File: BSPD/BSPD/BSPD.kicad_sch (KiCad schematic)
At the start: 10 parts, among them Q1 NMOS, U1 LM397, U2 LM397, U3 74AHC1G08, U4 74AHC1G02

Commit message: Timer and relay added/updated
Added timer circuit and 12v relay that we used from shutdown pcb
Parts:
- removed R1, R3: R_Small_US, symbol Device:R_Small_US
- added C1: 0.1u, symbol Device:C
- added K1: AZ943-1CH-12DE, AZ943-1CH_AMZ, symbol AZ943_1CH_12DE:AZ943-1CH-12DE
- added R5: 1M, symbol Device:R
- added R6: 523k, symbol Device:R
- added R7: 768k, symbol Device:R
- added RV1, RV2: 1k, symbol Device:R_Potentiometer
- added U5: LTC6994CS6-1-TRMPBF, TSOT-23_S6_LIT, symbol LTC6994:LTC6994CS6-1-TRMPBF
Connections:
- net GND: now also C1.2, R6.2, R7.2, U5.2 (GND)
- net at R2.1, U2.1 (-): now also RV2.3
- net at U4.4: now also U5.1 (IN)
- net at R4.1, U1.1 (-): now also RV1.3
- net at D1.1 (K): now also K1.5
- net at D1.2 (A), Q1.1 (D): now also K1.2
- net at Q1.2 (G): now also U5.6 (OUT)
- new net: R7.1, U5.3 (SET)
- new net: R5.2, R6.1, U5.4 (DIV)
- new net +5V: C1.1, R5.1, RV1.2, RV2.2, U5.5 (V+)
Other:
- moved on the sheet: D1, Q1, U4

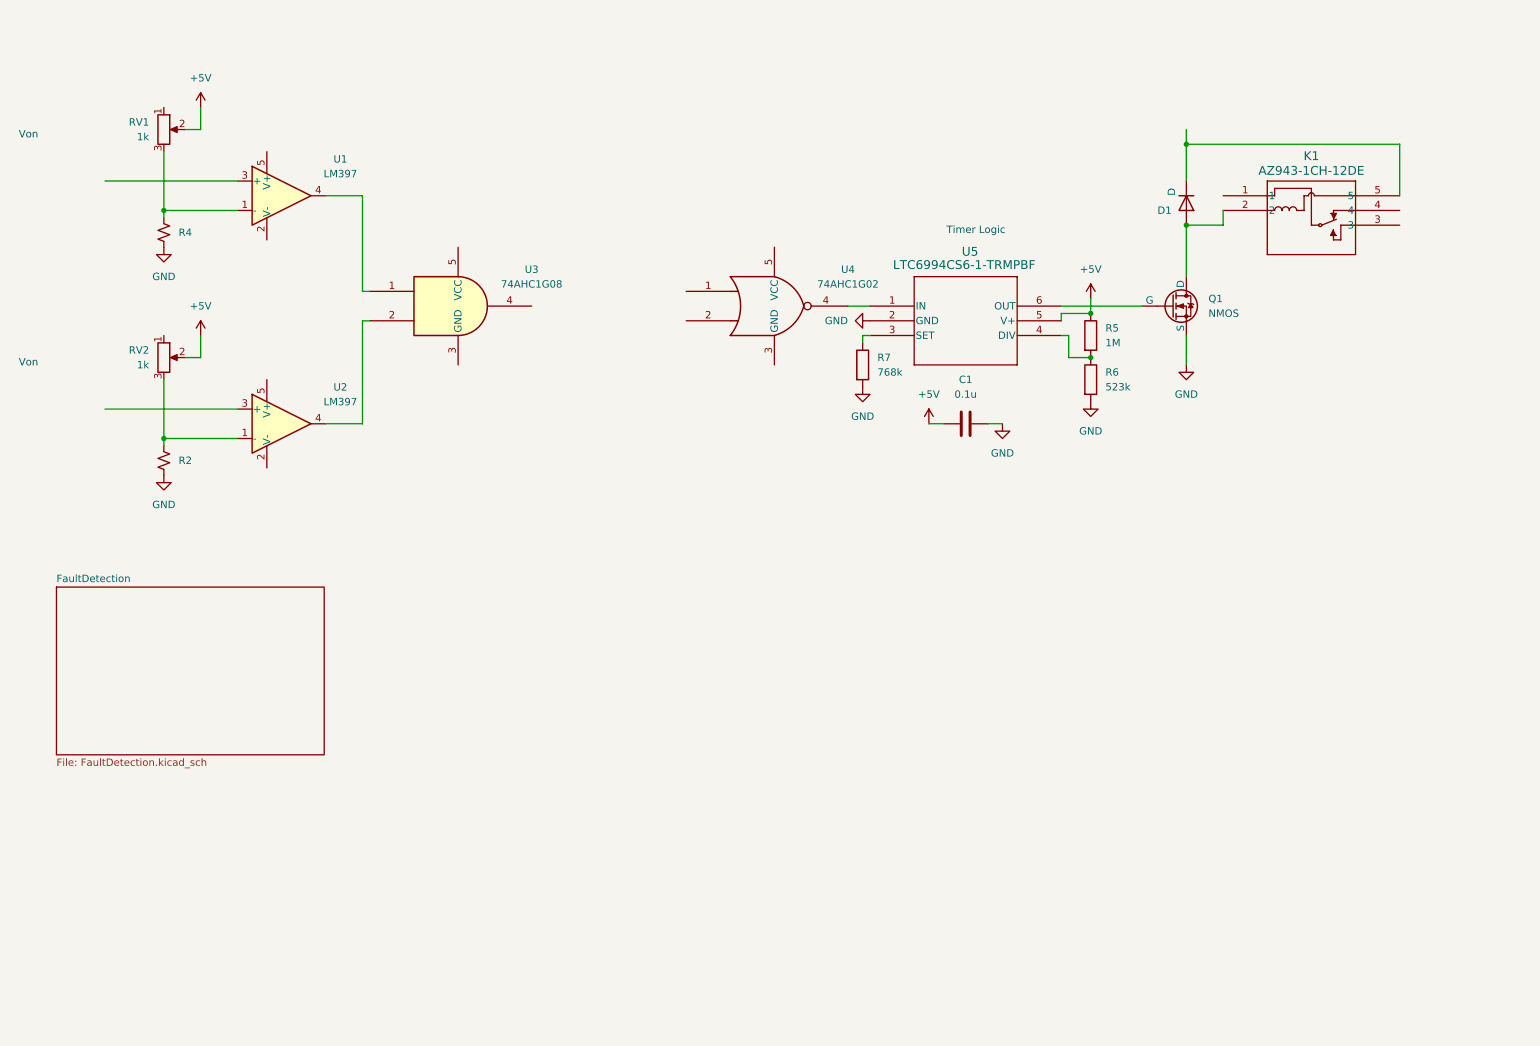
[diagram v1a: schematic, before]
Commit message: Relay Driver/Regulator/IO/LEDS/Comparator
Added relay driver, 5v regulator, debugging leds, 6 pin microfit connector for IO, and created footprint for TLV7012DDFR comparator we're using
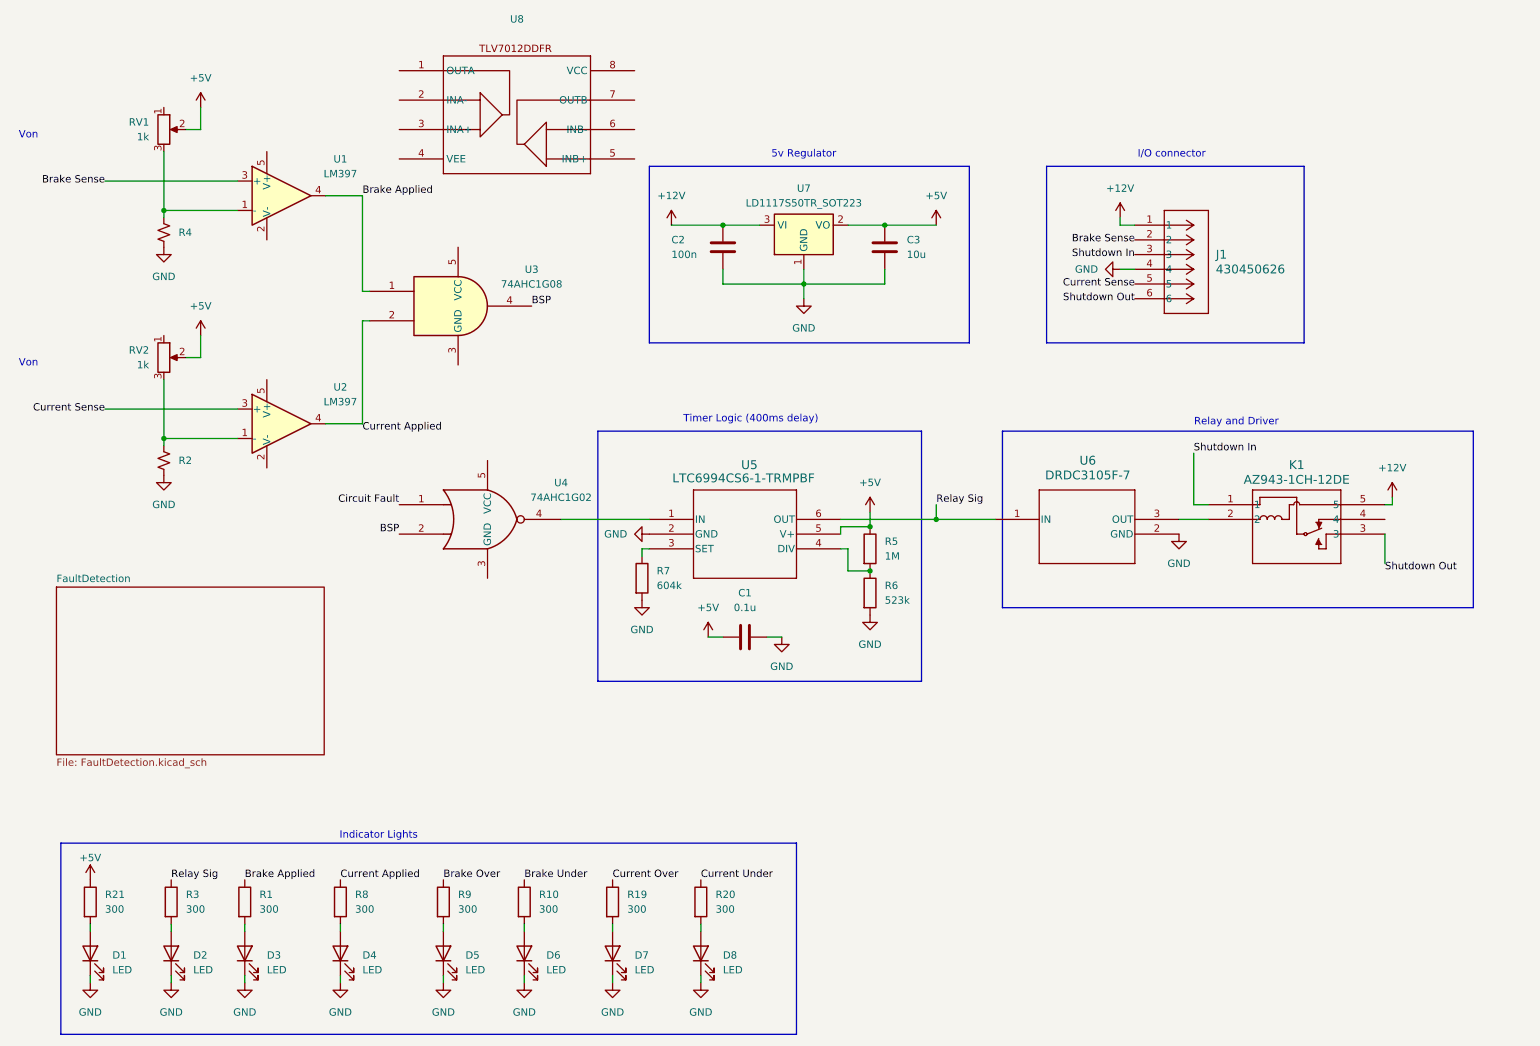
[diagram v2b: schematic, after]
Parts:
- removed D1: D, symbol Device:D
- removed Q1: NMOS, symbol Simulation_SPICE:NMOS
- added C2: 100n, symbol Device:C
- added C3: 10u, symbol Device:C
- added D1, D2, D3, D4, D5, D6, D7, D8: LED, symbol Device:LED
- added J1: 430450626, CONN_SD-43045-009_06_MOL, symbol Molex_430450626:430450626
- added R1, R10, R19, R20, R21, R3, R8, R9: 300, symbol Device:R
- added U6: DRDC3105F-7, SOT23_DIO, symbol DRDC3105:DRDC3105F-7
- added U7: LD1117S50TR_SOT223, Package_TO_SOT_SMD:SOT-223-3_TabPin2, symbol Regulator_Linear:LD1117S50TR_SOT223
- added U8: ~, symbol TLV7012DDFR:TLV7012DDFR
- R7: value 768k -> 604k
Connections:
- net +5V: now also C3.1, R21.1, U7.2 (VO)
- net GND: now also C2.2, C3.2, D1.1 (K), D2.1 (K), D3.1 (K), D4.1 (K), D5.1 (K), D6.1 (K), D7.1 (K), D8.1 (K), J1.4, U6.2 (GND), U7.1 (GND)
- net Current Sense: now reaches U2.3 (+)
- net Current Sense: now also J1.5
- net Current Applied: now reaches U2.4, U3.2
- net Current Applied: now also R8.1
- net Circuit Fault: now reaches U4.1
- net BSP: now reaches U4.2
- net BSP: now also U3.4
- net Brake Sense: now reaches U1.3 (+)
- net Brake Sense: now also J1.2
- net Brake Applied: now reaches U1.4, U3.1
- net Brake Applied: now also R1.1
- net +12V: now reaches K1.5
- net +12V: now also C2.1, J1.1, U7.3 (VI)
- net at K1.2: now also U6.3 (OUT)
- net Relay Sig: now reaches U5.6 (OUT)
- net Relay Sig: now also R3.1, U6.1 (IN)
- net Shutdown In: now reaches K1.1
- net Shutdown In: now also J1.3
- net Shutdown Out: now reaches K1.3
- net Shutdown Out: now also J1.6
- new net: D7.2 (A), R19.2
- new net: D8.2 (A), R20.2
- new net: D2.2 (A), R3.2
- new net: D6.2 (A), R10.2
- new net: D5.2 (A), R9.2
- new net: D4.2 (A), R8.2
- new net: D1.2 (A), R21.2
- new net: D3.2 (A), R1.2
- new net Brake Over: R9.1
- new net Brake Under: R10.1
- new net Current Over: R19.1
- new net Current Under: R20.1
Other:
- note added: "5v Regulator"
- note added: "I/O connector"
- note added: "Indicator Lights"
- note added: "Relay and Driver"
- note added: "Timer Logic (400ms delay)"
- note removed: "Timer Logic"
- title: (none) -> BSPD
- moved on the sheet: C1, K1, R5, R6, R7, U4, U5

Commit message: Added logic gate symbols
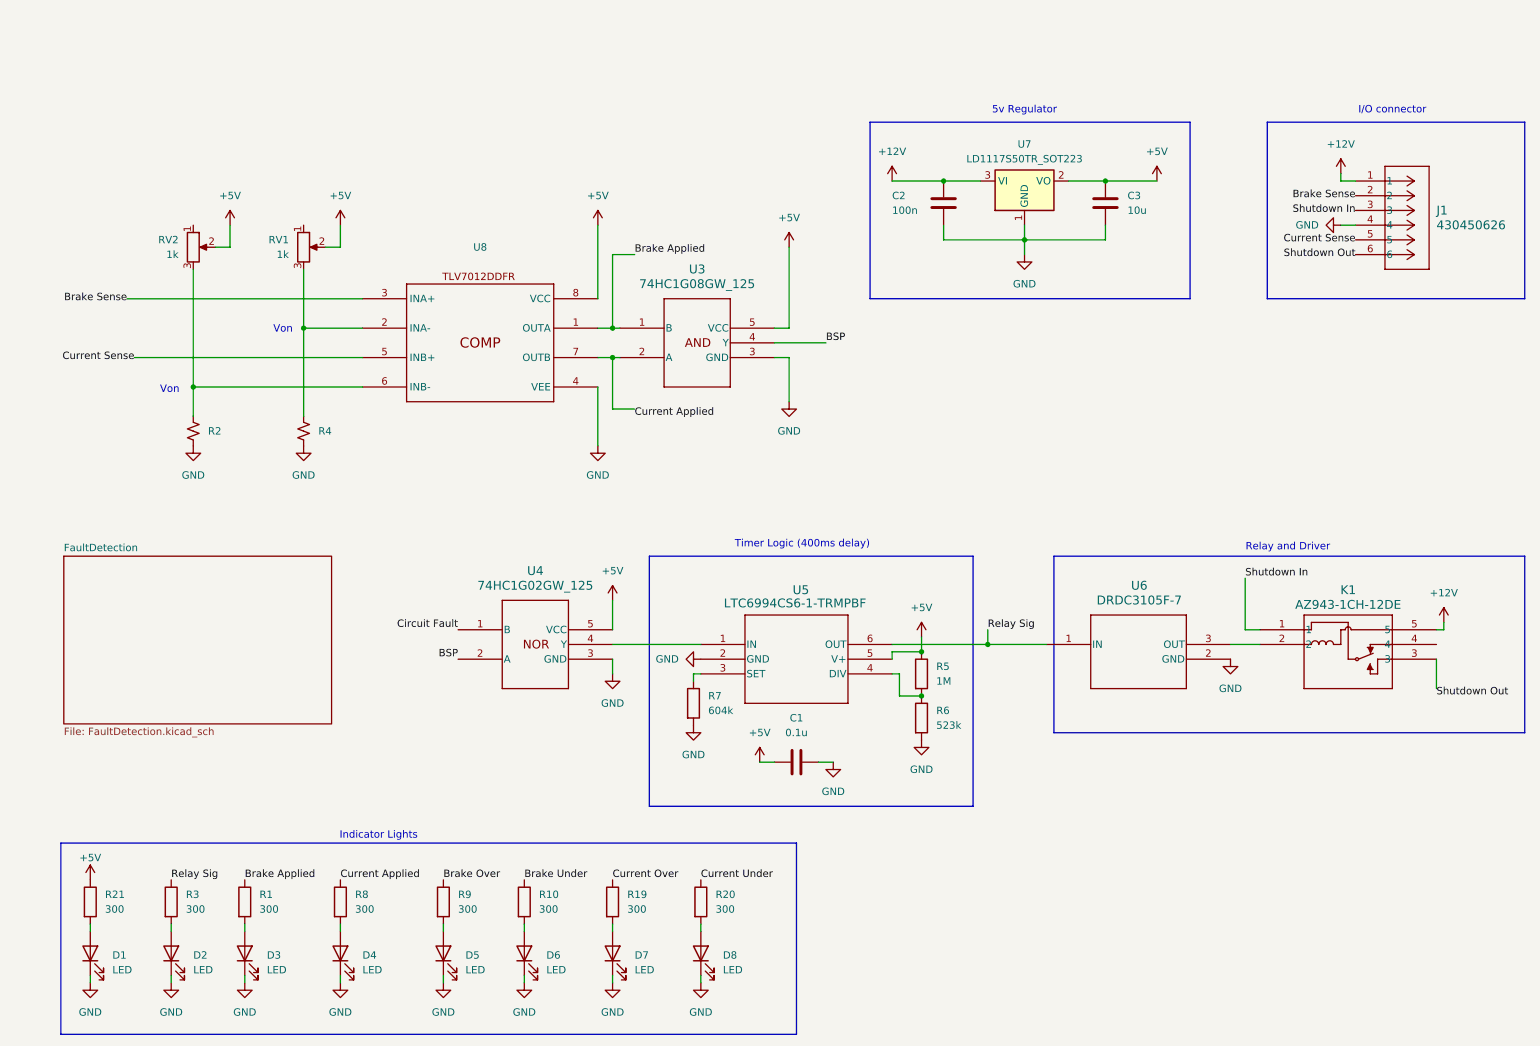
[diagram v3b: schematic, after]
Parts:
- removed U1, U2: LM397, Package_TO_SOT_SMD:SOT-23-5, symbol Comparator:LM397
- removed U3: 74AHC1G08, symbol 74xGxx:74AHC1G08
- removed U4: 74AHC1G02, symbol 74xGxx:74AHC1G02
- added U3: 74HC1G08GW_125, TSSOP5_SOT353-1_NEX, symbol 74HC1G_125:74HC1G08GW_125
- added U4: 74HC1G02GW_125, TSSOP5_SOT353-1_NEX, symbol 74HC1G_125:74HC1G02GW_125
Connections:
- net +5V: now also U8.8 (VCC), U3.5 (VCC), U4.5 (VCC)
- net BSP: now also U3.4 (Y), U4.2 (A)
- net Brake Applied: now also U8.1 (OUTA), U3.1 (B)
- net Brake Sense: now also U8.3 (INA+)
- net Circuit Fault: now also U4.1 (B)
- net Current Applied: now also U8.7 (OUTB), U3.2 (A)
- net Current Sense: now also U8.5 (INB+)
- net GND: now also U8.4 (VEE), U3.3 (GND), U4.3 (GND)
- net at R2.1, RV2.3: now also U8.6 (INB-)
- net at U5.1 (IN): now also U4.4 (Y)
- net at R4.1, RV1.3: now also U8.2 (INA-)
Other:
- moved on the sheet: C1, C2, C3, J1, K1, R2, R4, R5, R6, R7, RV1, RV2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

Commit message: Added decoupling caps
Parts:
- added C4, C5, C6: 0.1u, symbol Device:C
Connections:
- net +5V: now also C4.1, C5.1, C6.1
- net GND: now also C4.2, C5.2, C6.2
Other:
- moved on the sheet: U4

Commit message: Configure Falling Edge Delay
Swapped resistors on delay ic to detect a falling edge to align with other logic in circuit.
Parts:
- R5: value 1M -> 523k
- R6: value 523k -> 1M
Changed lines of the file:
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@@
 	(label "Brake Under"
 		(at 105.41 158.75 0)
+		(fields_autoplaced yes)
 		(effects
 			(font
@@
 	(label "Shutdown In"
 		(at 248.92 43.18 180)
+		(fields_autoplaced yes)
 		(effects
 			(font
@@
 	(label "Current Applied"
 		(at 124.46 77.47 0)
+		(fields_autoplaced yes)
 		(effects
 			(font
@@
 	(label "Current Sense"
 		(at 38.1 68.58 180)
+		(fields_autoplaced yes)
 		(effects
 			(font
@@
 	(label "Shutdown Out"
 		(at 248.92 50.8 180)
+		(fields_autoplaced yes)
 		(effects
 			(font
@@
 	(label "Brake Sense"
 		(at 36.83 58.42 180)
+		(fields_autoplaced yes)
 		(effects
 			(font
@@
 	(label "Relay Sig"
 		(at 185.42 115.57 0)
+		(fields_autoplaced yes)
 		(effects
 			(font
@@
 	(label "Circuit Fault"
 		(at 86.36 115.57 180)
+		(fields_autoplaced yes)
 		(effects
 			(font
@@
 	(label "Current Sense"
 		(at 248.92 48.26 180)
+		(fields_autoplaced yes)
 		(effects
 			(font
@@
 	(label "Shutdown In"
 		(at 229.87 106.68 0)
+		(fields_autoplaced yes)
 		(effects
 			(font
@@
 	(label "Current Under"
 		(at 135.89 158.75 0)
+		(fields_autoplaced yes)
 		(effects
 			(font
@@
 	(label "Shutdown Out"
 		(at 262.89 125.73 0)
+		(fields_autoplaced yes)
 		(effects
 			(font
@@
 	(label "Brake Over"
 		(at 91.44 158.75 0)
+		(fields_autoplaced yes)
 		(effects
 			(font
@@
 	(label "Current Over"
 		(at 120.65 158.75 0)
+		(fields_autoplaced yes)
 		(effects
 			(font
@@
 	(label "Current Applied"
 		(at 73.66 158.75 0)
+		(fields_autoplaced yes)
 		(effects
 			(font
@@
 	(label "BSP"
 		(at 157.48 66.04 0)
+		(fields_autoplaced yes)
 		(effects
 			(font
@@
 	(label "Brake Sense"
 		(at 248.92 40.64 180)
+		(fields_autoplaced yes)
 		(effects
 			(font
@@
 	(label "Brake Applied"
 		(at 57.15 158.75 0)
+		(fields_autoplaced yes)
 		(effects
 			(font
@@
 	(label "BSP"
 		(at 86.36 120.65 180)
+		(fields_autoplaced yes)
 		(effects
 			(font
@@
 	(label "Brake Applied"
 		(at 124.46 50.8 0)
+		(fields_autoplaced yes)
 		(effects
 			(font
@@
 	(label "Relay Sig"
 		(at 44.45 158.75 0)
+		(fields_autoplaced yes)
 		(effects
 			(font
@@
 			)
 		)
-		(property "Value" "1M"
+		(property "Value" "523k"
 			(at 176.53 124.4599 0)
 			(effects
@@
 			)
 		)
-		(property "Value" "523k"
+		(property "Value" "1M"
 			(at 176.53 132.0799 0)
 			(effects
